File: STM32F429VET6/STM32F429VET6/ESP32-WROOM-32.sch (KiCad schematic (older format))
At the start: 10 parts

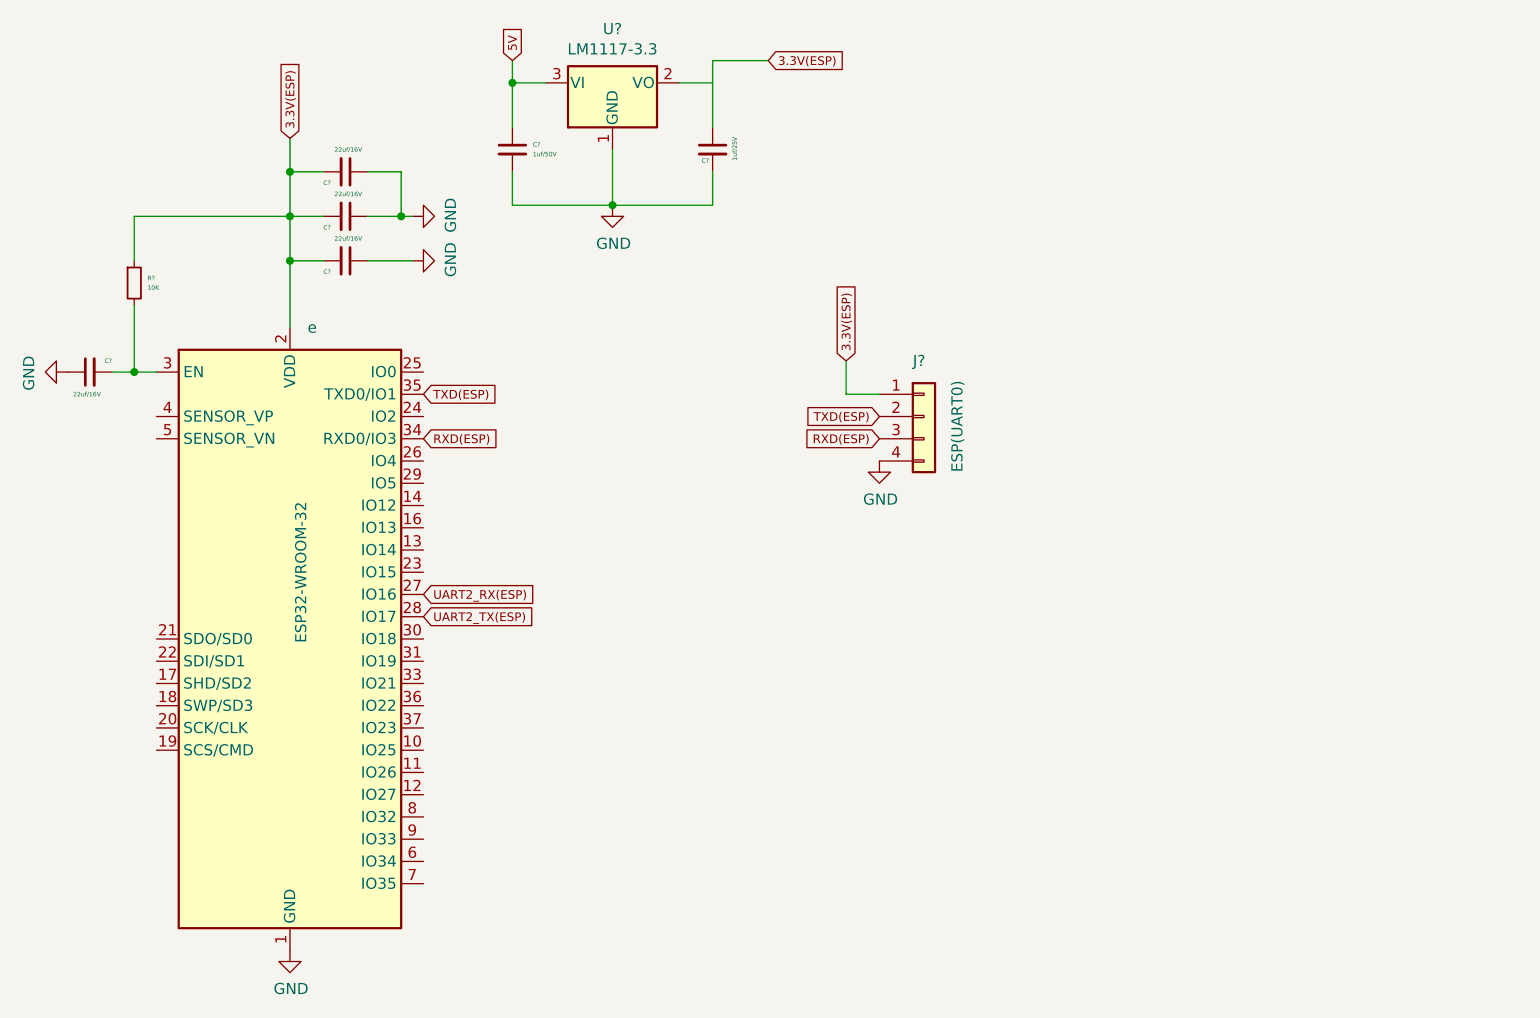
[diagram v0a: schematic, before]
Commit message: Completed GPS module connection
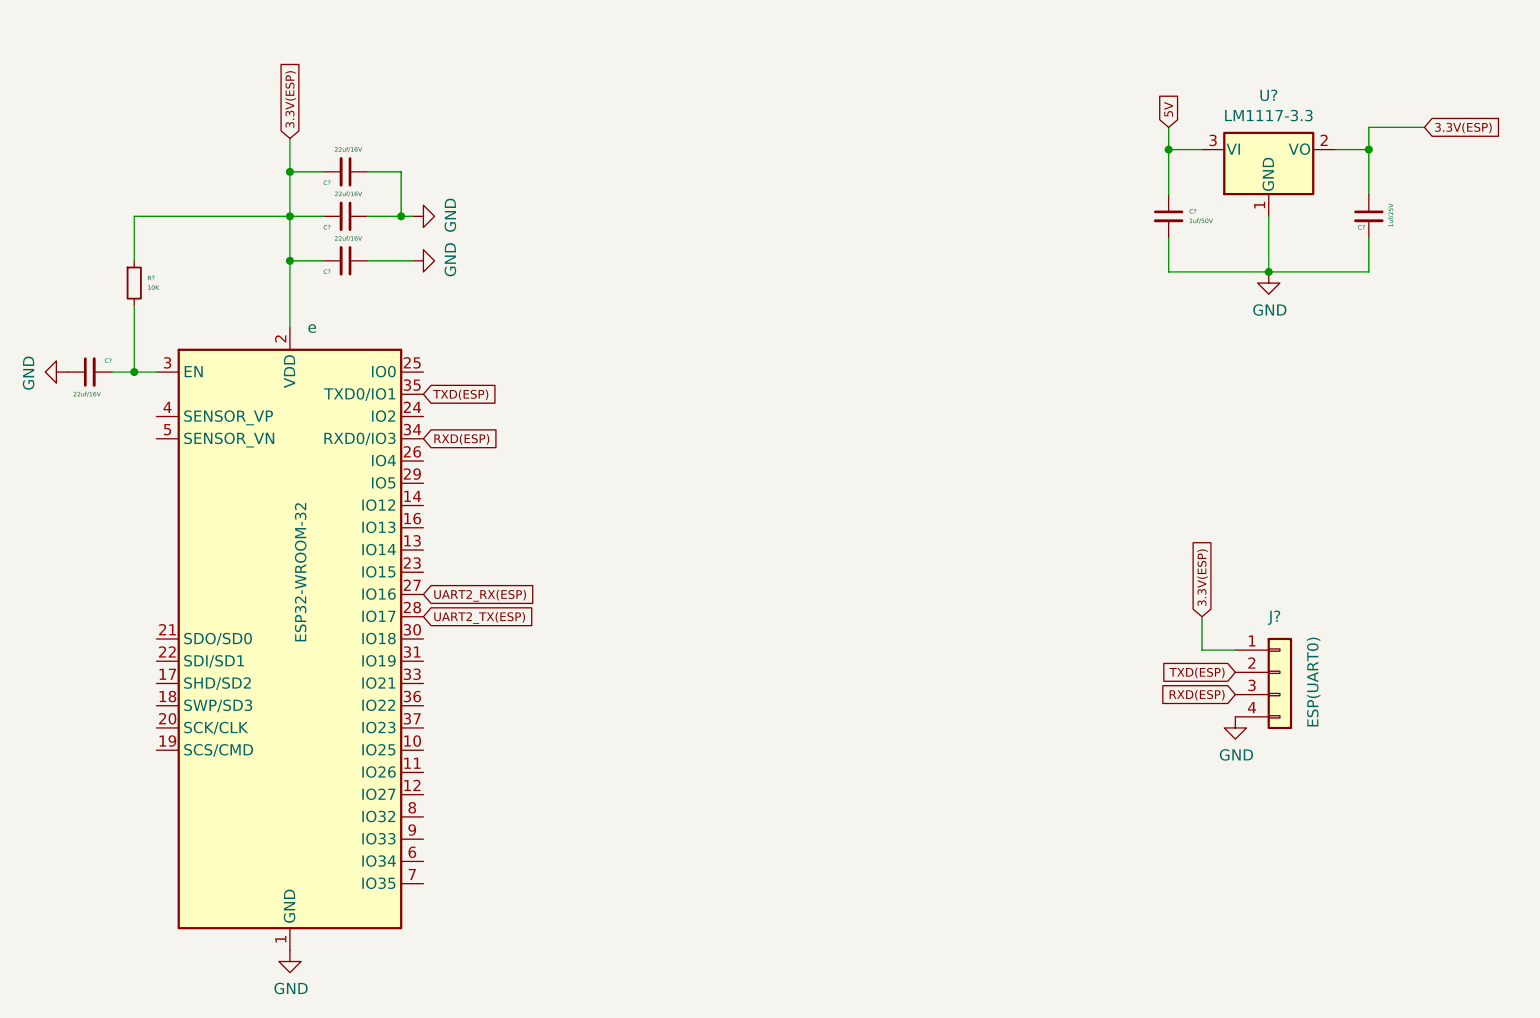
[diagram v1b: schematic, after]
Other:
- moved on the sheet: C?, J?, U?
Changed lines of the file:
@@
 $Descr A4 11693 8268
 encoding utf-8
-Sheet 3 4
+Sheet 3 5
 Title ""
 Date ""
@@
 L Device:C_Small C?
 U 1 1 6092C4E8
-P 5350 1150
+P 8300 1450
 AR Path="/5FD5E119/6092C4E8" Ref="C?"  Part="1"
 AR Path="/6092C4E8" Ref="C?"  Part="1"
 AR Path="/5FD5E119/60922ED4/6092C4E8" Ref="C?"  Part="1"
-F 0 "C?" H 5442 1172 20  0000 L CNN
-F 1 "1uf/50V" H 5442 1129 20  0000 L CNN
-F 2 "Capacitor_SMD:C_0805_2012Metric_Pad1.15x1.40mm_HandSolder" H 5350 1150 50  0001 C CNN
-F 3 "~" H 5350 1150 50  0001 C CNN
-	1    5350 1150
-	1    0    0    -1
-$EndComp
-Wire Wire Line
-	5350 850  5350 1050
-Wire Wire Line
-	5350 1250 5350 1400
-Text GLabel 5350 750  1    39   Input ~ 0
+F 0 "C?" H 8392 1472 20  0000 L CNN
+F 1 "1uf/50V" H 8392 1429 20  0000 L CNN
+F 2 "Capacitor_SMD:C_0805_2012Metric_Pad1.15x1.40mm_HandSolder" H 8300 1450 50  0001 C CNN
+F 3 "~" H 8300 1450 50  0001 C CNN
+	1    8300 1450
+	1    0    0    -1
+$EndComp
+Wire Wire Line
+	8300 1150 8300 1350
+Wire Wire Line
+	8300 1550 8300 1700
+Text GLabel 8300 1050 1    39   Input ~ 0
 5V
 Wire Wire Line
-	5350 750  5350 850
-Connection ~ 5350 850
+	8300 1050 8300 1150
+Connection ~ 8300 1150
 $Comp
 L Regulator_Linear:LM1117-3.3 U?
 U 1 1 6092C4F5
-P 5800 850
+P 8750 1150
 AR Path="/6092C4F5" Ref="U?"  Part="1"
 AR Path="/5FD5E119/60922ED4/6092C4F5" Ref="U?"  Part="1"
-F 0 "U?" H 5800 1092 50  0000 C CNN
-F 1 "LM1117-3.3" H 5800 1001 50  0000 C CNN
-F 2 "" H 5800 850 50  0001 C CNN
-F 3 "http://www.ti.com/lit/ds/symlink/lm1117.pdf" H 5800 850 50  0001 C CNN
-	1    5800 850
-	1    0    0    -1
-$EndComp
-Wire Wire Line
-	5350 850  5500 850
-Wire Wire Line
-	5800 1150 5800 1400
-Wire Wire Line
-	5800 1400 5350 1400
+F 0 "U?" H 8750 1392 50  0000 C CNN
+F 1 "LM1117-3.3" H 8750 1301 50  0000 C CNN
+F 2 "" H 8750 1150 50  0001 C CNN
+F 3 "http://www.ti.com/lit/ds/symlink/lm1117.pdf" H 8750 1150 50  0001 C CNN
+	1    8750 1150
+	1    0    0    -1
+$EndComp
+Wire Wire Line
+	8300 1150 8450 1150
+Wire Wire Line
+	8750 1450 8750 1700
+Wire Wire Line
+	8750 1700 8300 1700
 $Comp
 L Device:C_Small C?
 U 1 1 6092C4FF
-P 6250 1150
+P 9200 1450
 AR Path="/5FD5E119/6092C4FF" Ref="C?"  Part="1"
 AR Path="/6092C4FF" Ref="C?"  Part="1"
 AR Path="/5FD5E119/60922ED4/6092C4FF" Ref="C?"  Part="1"
-F 0 "C?" H 6200 1100 20  0000 L CNN
-F 1 "1uf/25V" V 6350 1100 20  0000 L CNN
-F 2 "Capacitor_SMD:C_0805_2012Metric_Pad1.15x1.40mm_HandSolder" H 6250 1150 50  0001 C CNN
-F 3 "~" H 6250 1150 50  0001 C CNN
-	1    6250 1150
-	1    0    0    -1
-$EndComp
-Wire Wire Line
-	6100 850  6250 850
-Wire Wire Line
-	6250 850  6250 1050
-Wire Wire Line
-	6250 1250 6250 1400
-Wire Wire Line
-	6250 1400 5800 1400
-Connection ~ 5800 1400
-Wire Wire Line
-	6250 850  6250 750
-Text GLabel 6500 750  2    39   Input ~ 0
+F 0 "C?" H 9150 1400 20  0000 L CNN
+F 1 "1uf/25V" V 9300 1400 20  0000 L CNN
+F 2 "Capacitor_SMD:C_0805_2012Metric_Pad1.15x1.40mm_HandSolder" H 9200 1450 50  0001 C CNN
+F 3 "~" H 9200 1450 50  0001 C CNN
+	1    9200 1450
+	1    0    0    -1
+$EndComp
+Wire Wire Line
+	9050 1150 9200 1150
+Wire Wire Line
+	9200 1150 9200 1350
+Wire Wire Line
+	9200 1550 9200 1700
+Wire Wire Line
+	9200 1700 8750 1700
+Connection ~ 8750 1700
+Wire Wire Line
+	9200 1150 9200 1050
+Text GLabel 9450 1050 2    39   Input ~ 0
 3.3V(ESP)
 Wire Wire Line
-	6500 750  6250 750
+	9450 1050 9200 1050
 Text GLabel 4350 1100 1    39   Input ~ 0
 3.3V(ESP)
@@
 L power:GND #PWR?
 U 1 1 6092F0EB
-P 5800 1400
+P 8750 1700
 AR Path="/5FD5E119/6092F0EB" Ref="#PWR?"  Part="1"
 AR Path="/5FD5E119/60922ED4/6092F0EB" Ref="#PWR?"  Part="1"
-F 0 "#PWR?" H 5800 1150 50  0001 C CNN
-F 1 "GND" H 5805 1227 50  0000 C CNN
-F 2 "" H 5800 1400 50  0001 C CNN
-F 3 "" H 5800 1400 50  0001 C CNN
-	1    5800 1400
+F 0 "#PWR?" H 8750 1450 50  0001 C CNN
+F 1 "GND" H 8755 1527 50  0000 C CNN
+F 2 "" H 8750 1700 50  0001 C CNN
+F 3 "" H 8750 1700 50  0001 C CNN
+	1    8750 1700
 	1    0    0    -1
 $EndComp
@@
 L Connector_Generic:Conn_01x04 J?
 U 1 1 5FD7648D
-P 7200 2350
-F 0 "J?" H 7150 2600 50  0000 L CNN
-F 1 "ESP(UART0)" V 7350 2100 50  0000 L CNN
-F 2 "Connector_JST:JST_EH_B4B-EH-A_1x04_P2.50mm_Vertical" H 7200 2350 50  0001 C CNN
-F 3 "~" H 7200 2350 50  0001 C CNN
-	1    7200 2350
-	1    0    0    -1
-$EndComp
-Text GLabel 6850 2100 1    39   Input ~ 0
+P 8800 3500
+F 0 "J?" H 8750 3750 50  0000 L CNN
+F 1 "ESP(UART0)" V 8950 3250 50  0000 L CNN
+F 2 "Connector_JST:JST_EH_B4B-EH-A_1x04_P2.50mm_Vertical" H 8800 3500 50  0001 C CNN
+F 3 "~" H 8800 3500 50  0001 C CNN
+	1    8800 3500
+	1    0    0    -1
+$EndComp
+Text GLabel 8450 3250 1    39   Input ~ 0
 3.3V(ESP)
 Wire Wire Line
-	6850 2250 6850 2100
-Wire Wire Line
-	7000 2250 6850 2250
-Text GLabel 7000 2350 0    39   Input ~ 0
+	8450 3400 8450 3250
+Wire Wire Line
+	8600 3400 8450 3400
+Text GLabel 8600 3500 0    39   Input ~ 0
 TXD(ESP)
-Text GLabel 7000 2450 0    39   Input ~ 0
+Text GLabel 8600 3600 0    39   Input ~ 0
 RXD(ESP)
 $Comp
 L power:GND #PWR?
 U 1 1 5FD78B7C
-P 7000 2550
+P 8600 3700
 AR Path="/5FD5E119/5FD78B7C" Ref="#PWR?"  Part="1"
 AR Path="/5FD5E119/60922ED4/5FD78B7C" Ref="#PWR?"  Part="1"
-F 0 "#PWR?" H 7000 2300 50  0001 C CNN
-F 1 "GND" H 7005 2377 50  0000 C CNN
-F 2 "" H 7000 2550 50  0001 C CNN
-F 3 "" H 7000 2550 50  0001 C CNN
-	1    7000 2550
-	1    0    0    -1
-$EndComp
+F 0 "#PWR?" H 8600 3450 50  0001 C CNN
+F 1 "GND" H 8605 3527 50  0000 C CNN
+F 2 "" H 8600 3700 50  0001 C CNN
+F 3 "" H 8600 3700 50  0001 C CNN
+	1    8600 3700
+	1    0    0    -1
+$EndComp
+Connection ~ 9200 1150
 $EndSCHEMATC
